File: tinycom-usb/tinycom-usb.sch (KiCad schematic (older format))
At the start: 60 parts, among them J1 MICRO_SD_HINGE, P1 CONN_02X10, P2 CONN_02X10, P3 USB_A, P4 USB_OTG, U1 SY8008BAAC, U2 AXP209, U3 SY8008BAAC, U4 RTL8188, U5 rainsun-antenna

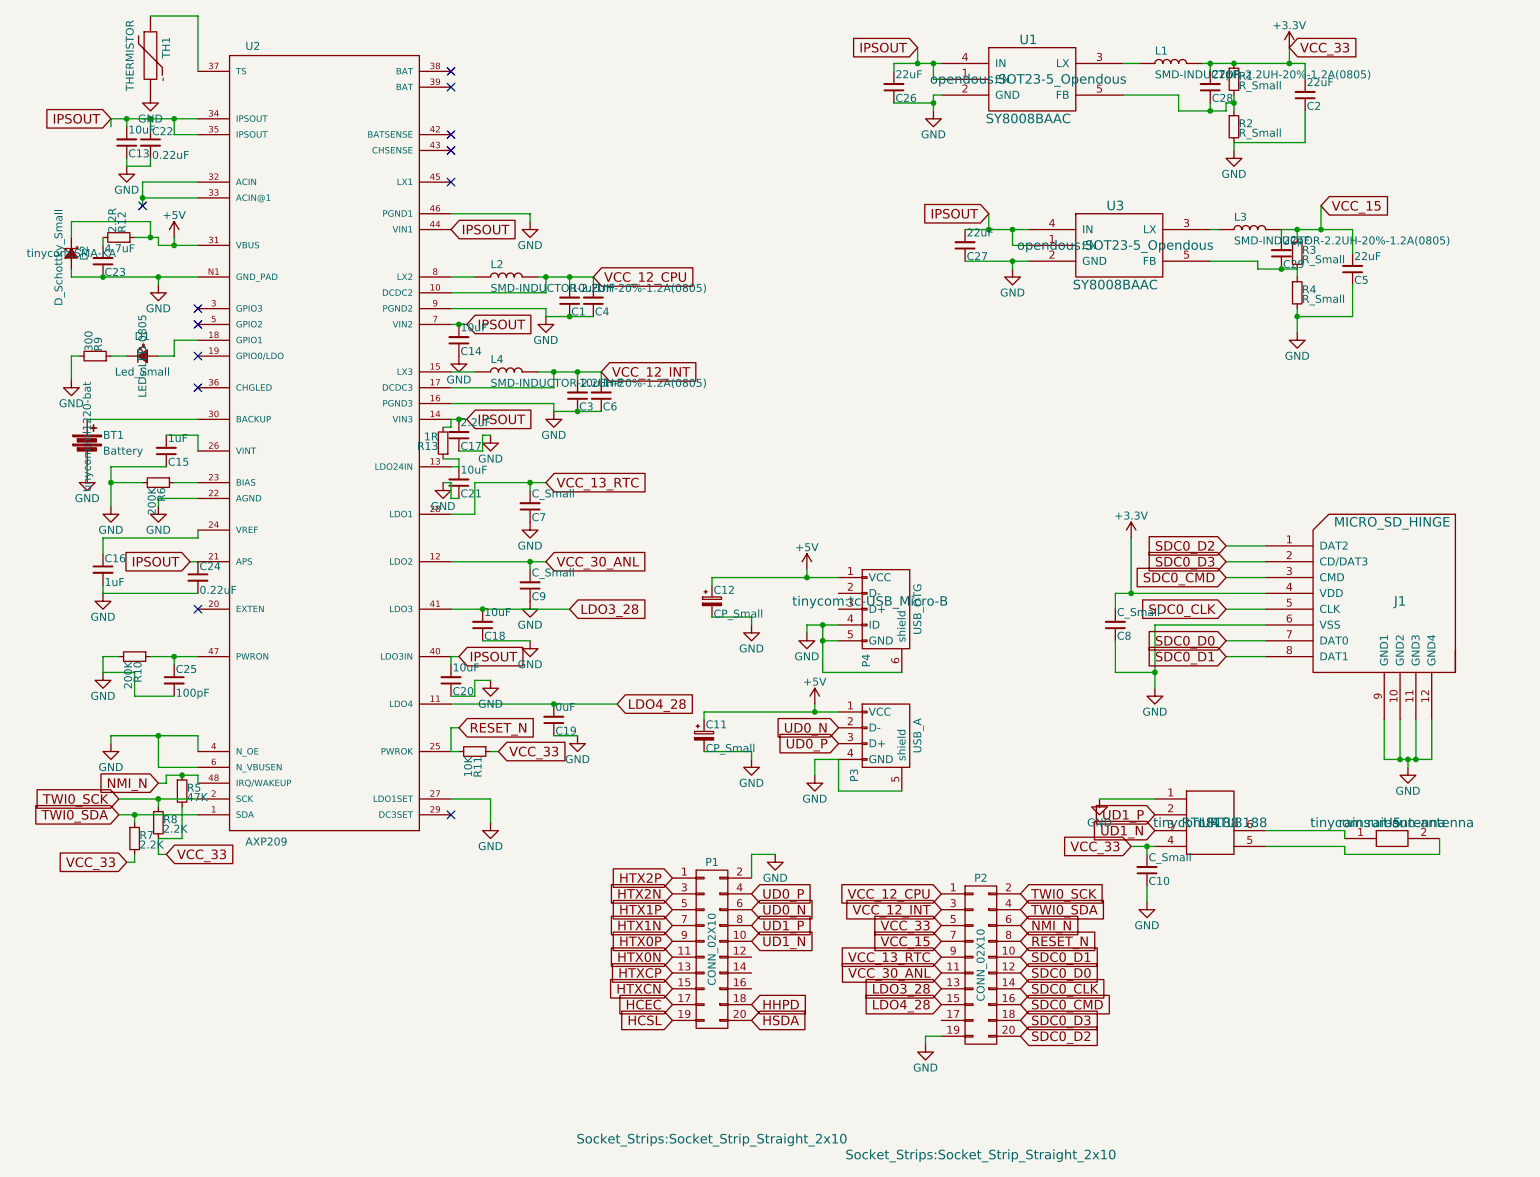
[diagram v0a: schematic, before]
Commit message: improve tinycom-usb (usb connector+antenna)
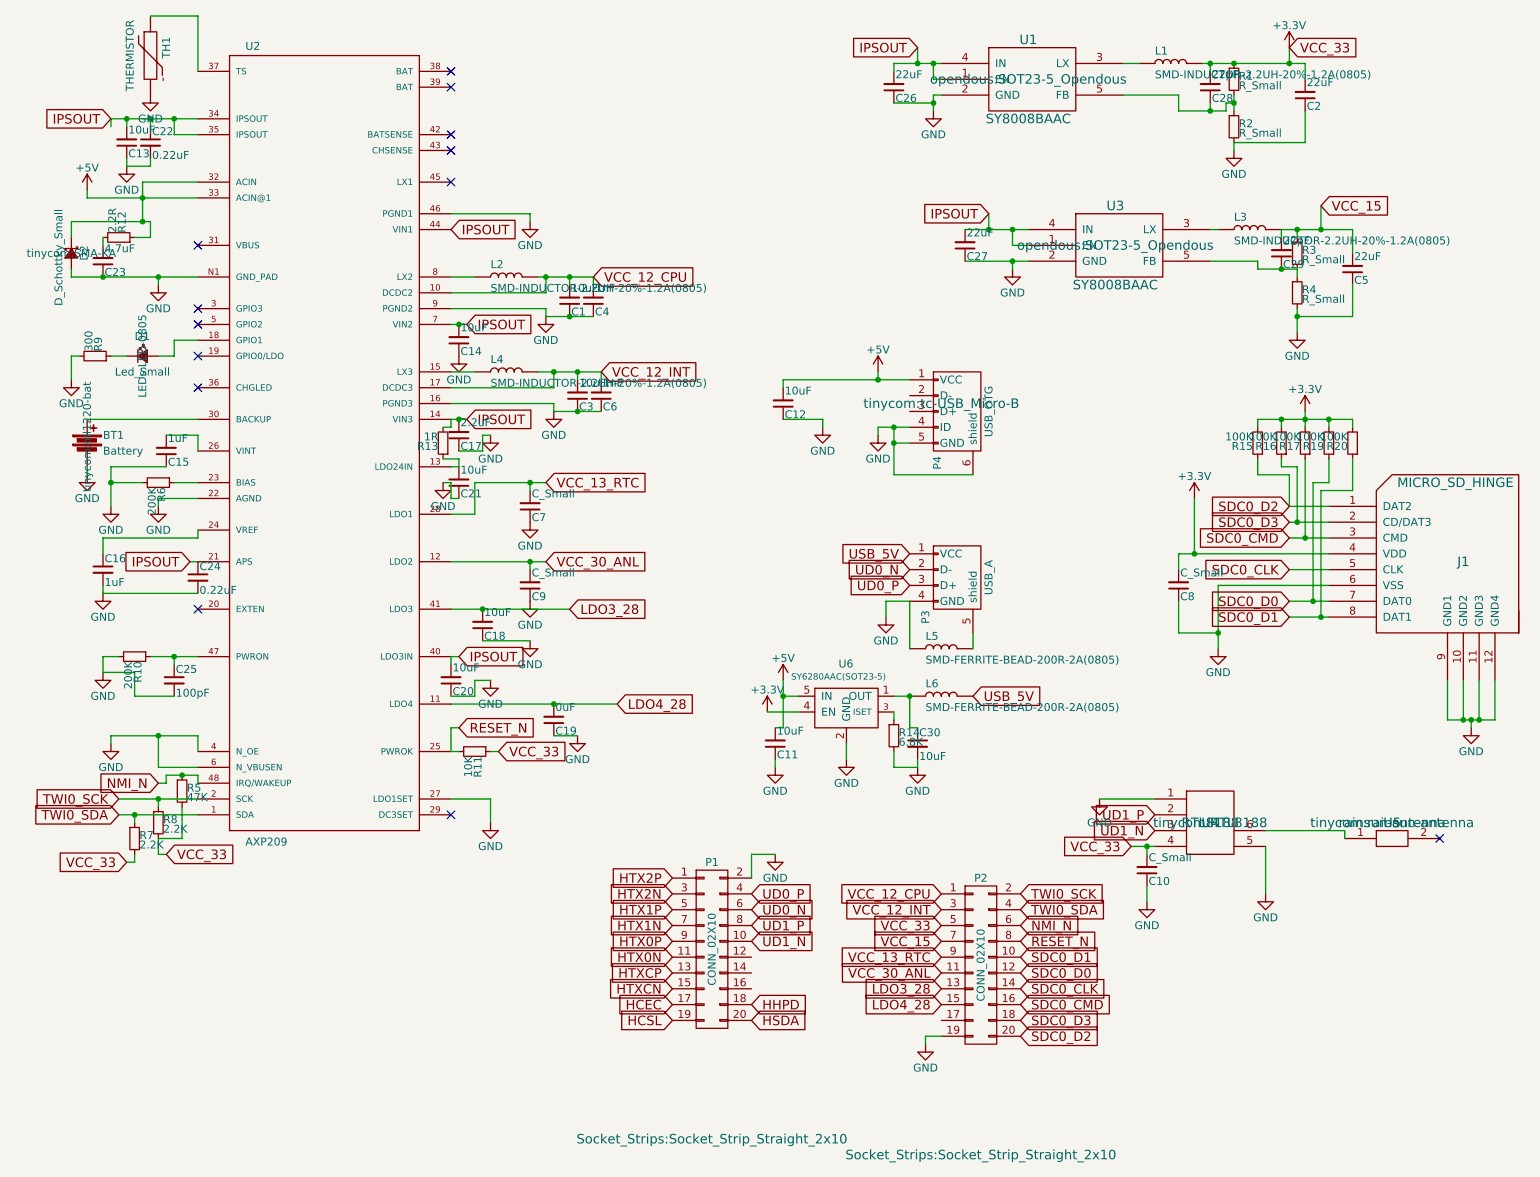
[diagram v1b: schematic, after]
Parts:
- removed C11, C12: CP_Small, Capacitors_Tantalum_SMD:TantalC_SizeA_EIA-3216_Reflow, symbol CP_Small
- added C11, C12, C30: 10uF, Capacitors_SMD:C_0805, symbol C_Small
- added L5, L6: SMD-FERRITE-BEAD-200R-2A(0805), OPL-Inductor-L0805, symbol SMD-FERRITE-BEAD-200R-2A(0805)
- added R14: 6.8K, Resistors_SMD:R_0805, symbol R_Small
- added R15, R16, R17, R19, R20: 100K, Resistors_SMD:R_0805, symbol R_Small
- added U6: SY6280AAC(SOT23-5), opendous:SOT23-5_Opendous, symbol SY6280AAC(SOT23-5)
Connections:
- net +3V3: now also R15.2, R16.2, R17.2, R19.2, R20.2, U6.4 (EN)
- net +5V: now also U2.32 (ACIN), U2.33 (ACIN@1), C11.2, C12.2, U6.5 (IN); no longer P3.1 (VCC), U2.31 (VBUS)
- net GND: now also U4.5, C11.1, C12.1, C30.2, L5.1, R14.2, U6.2 (GND); no longer P3.5 (shield)
- net SDC0_CMD: now also R17.1
- net SDC0_D0: now also R19.1
- net SDC0_D1: now also R20.1
- net SDC0_D2: now also R15.1
- net SDC0_D3: now also R16.1
- net at U5.2: no longer U4.5
- new net: L5.2, P3.5 (shield)
- new net: C30.1, L6.1, U6.1 (OUT)
- new net: R14.1, U6.3 (ISET)
- new net USB_5V: L6.2, P3.1 (VCC)
- no-connect marks 12 -> 13
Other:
- moved on the sheet: C8, J1, P3, P4

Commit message: fix tinycom-usb exten
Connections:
- net IPSOUT: no longer U1.1 (EN)
- net EXTEN: now reaches U2.20 (EXTEN)
- net EXTEN: now also U1.1 (EN)
- no-connect marks 13 -> 12
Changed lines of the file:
@@
 Text GLabel 1350 4150 0    60   Input ~ 0
 IPSOUT
-NoConn ~ 1400 4450
 $Comp
 L R_Small R6
@@
 Wire Wire Line
 	6550 2250 6550 2300
-Wire Wire Line
-	6100 1100 6050 1100
-Wire Wire Line
-	6050 1100 6050 1000
-Connection ~ 6050 1000
 Wire Wire Line
 	4900 6000 5050 6000
@@
 	1    0    0    1
 $EndComp
+Text GLabel 1400 4450 0    60   Input ~ 0
+EXTEN
+Text GLabel 5600 1100 0    60   Input ~ 0
+EXTEN
+Wire Wire Line
+	5600 1100 6100 1100
 $EndSCHEMATC

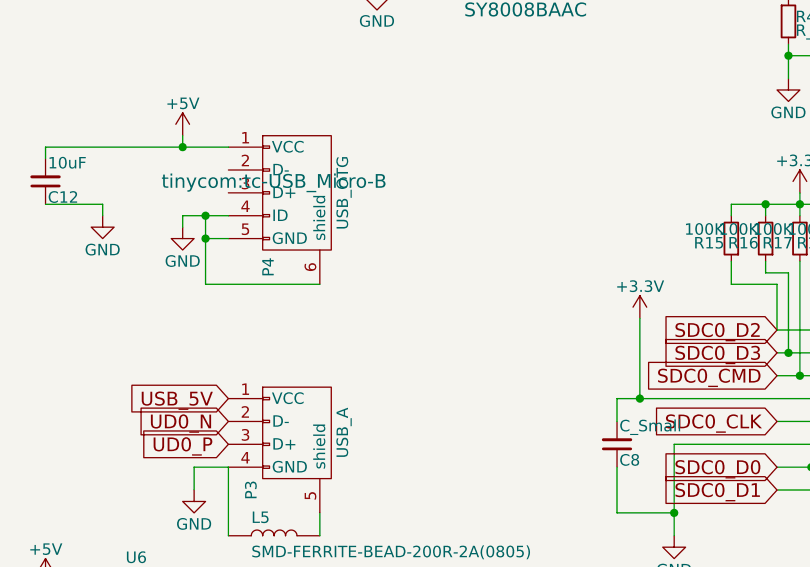
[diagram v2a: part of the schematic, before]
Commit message: improve tinycom-usb
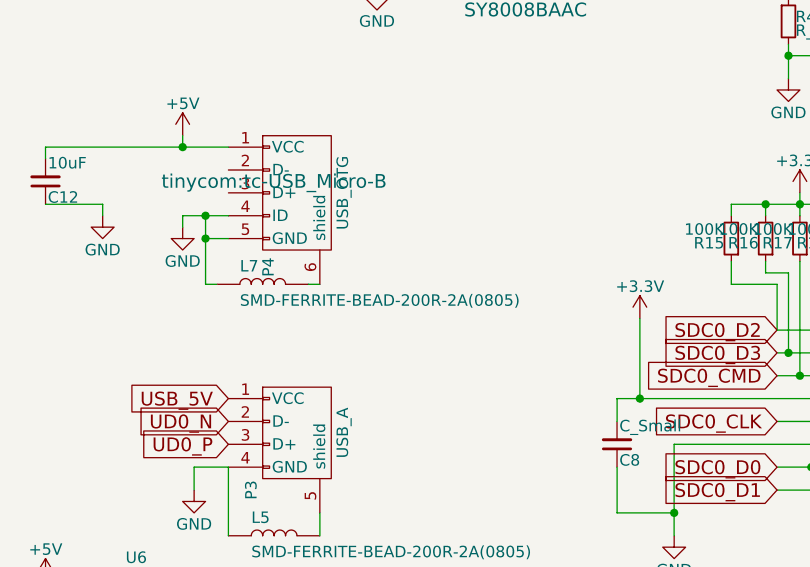
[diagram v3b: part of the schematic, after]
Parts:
- added L7: SMD-FERRITE-BEAD-200R-2A(0805), OPL-Inductor-L0805, symbol SMD-FERRITE-BEAD-200R-2A(0805)
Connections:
- net GND: now also L7.1; no longer P4.6 (shield)
- new net: L7.2, P4.6 (shield)
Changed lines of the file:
@@
 	5800 3300 5800 3600
 Connection ~ 5800 3300
-Wire Wire Line
-	5800 3600 6300 3600
 Connection ~ 5800 3400
 Wire Wire Line
@@
 Wire Wire Line
 	5600 1100 6100 1100
+$Comp
+L SMD-FERRITE-BEAD-200R-2A(0805) L7
+U 1 1 570B249A
+P 6050 3600
+F 0 "L7" H 5950 3650 50  0000 L BNN
+F 1 "SMD-FERRITE-BEAD-200R-2A(0805)" H 5950 3500 50  0000 L BNN
+F 2 "OPL-Inductor-L0805" H 6050 3750 50  0001 C CNN
+F 3 "" H 6050 3600 60  0000 C CNN
+F 4 "303030033" H 6050 3600 60  0001 C CNN "Desc"
+F 5 "NIL" H 6050 3600 60  0001 C CNN "MFG NO"
+F 6 "NIL" H 6050 3600 60  0001 C CNN "MFR"
+F 7 "NIL" H 6050 3600 60  0001 C CNN "Notes"
+	1    6050 3600
+	1    0    0    -1
+$EndComp
+Wire Wire Line
+	5800 3600 5850 3600
+Wire Wire Line
+	6300 3600 6250 3600
 $EndSCHEMATC

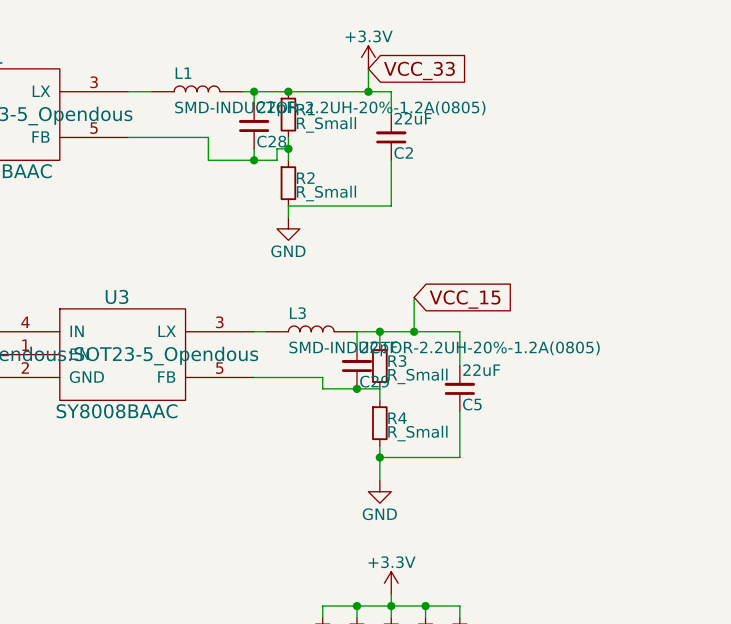
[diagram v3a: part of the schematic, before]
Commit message: improve tinycom-usb
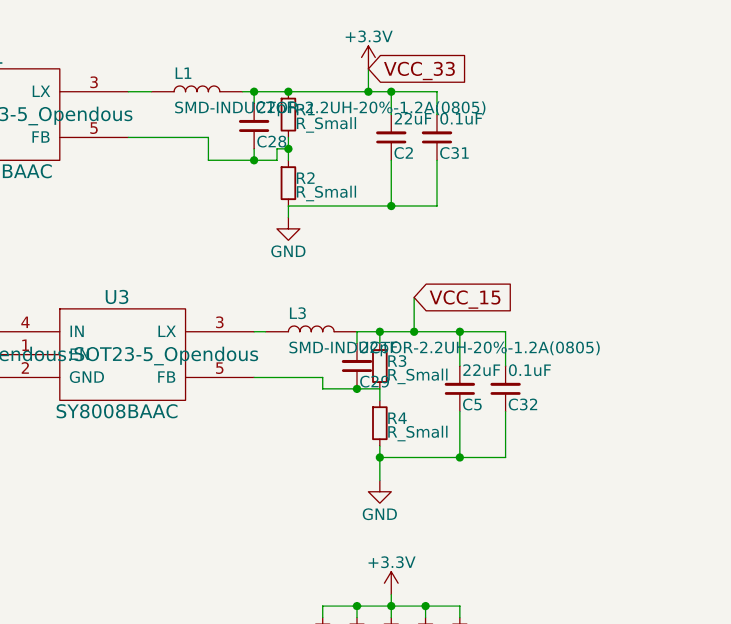
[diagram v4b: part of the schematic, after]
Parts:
- added C31, C32: 0.1uF, Capacitors_SMD:C_0805, symbol C_Small
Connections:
- net +3V3: now also C31.2
- net GND: now also C31.1, C32.1
- net VCC_15: now also C32.2
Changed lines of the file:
@@
 	8400 1300 8400 1500
 Wire Wire Line
-	8400 1500 7950 1500
+	7950 1500 8600 1500
 Wire Wire Line
 	7350 1000 7250 1000
@@
 	7800 2050 7850 2050
 Wire Wire Line
-	8250 2050 8700 2050
+	8250 2050 8900 2050
 Wire Wire Line
 	8350 2050 8350 2100
@@
 	8700 2400 8700 2600
 Wire Wire Line
-	8700 2600 8350 2600
+	8350 2600 8900 2600
 Wire Wire Line
 	8350 2550 8350 2700
@@
 	5800 1000 6100 1000
 Wire Wire Line
-	7750 1000 8400 1000
+	7750 1000 8600 1000
 Wire Wire Line
 	3000 2350 3150 2350
@@
 Wire Wire Line
 	6300 3600 6250 3600
+$Comp
+L C_Small C31
+U 1 1 570B7756
+P 8600 1200
+F 0 "C31" H 8610 1270 50  0000 L CNN
+F 1 "0.1uF" H 8610 1120 50  0000 L CNN
+F 2 "Capacitors_SMD:C_0805" H 8600 1200 60  0001 C CNN
+F 3 "" H 8600 1200 60  0000 C CNN
+	1    8600 1200
+	1    0    0    1
+$EndComp
+Wire Wire Line
+	8600 1000 8600 1100
+Connection ~ 8400 1000
+Wire Wire Line
+	8600 1500 8600 1300
+Connection ~ 8400 1500
+$Comp
+L C_Small C32
+U 1 1 570B7CE7
+P 8900 2300
+F 0 "C32" H 8910 2370 50  0000 L CNN
+F 1 "0.1uF" H 8910 2220 50  0000 L CNN
+F 2 "Capacitors_SMD:C_0805" H 8900 2300 60  0001 C CNN
+F 3 "" H 8900 2300 60  0000 C CNN
+	1    8900 2300
+	1    0    0    1
+$EndComp
+Wire Wire Line
+	8900 2050 8900 2200
+Connection ~ 8700 2050
+Wire Wire Line
+	8900 2600 8900 2400
+Connection ~ 8700 2600
 $EndSCHEMATC
